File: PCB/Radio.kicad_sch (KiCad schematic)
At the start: 31 parts, among them J701 Conn_Coaxial, U701 SX1262, U702 SKY13453-385LF, Y701 NX2016SA-32MHZ-STD-CZS-5

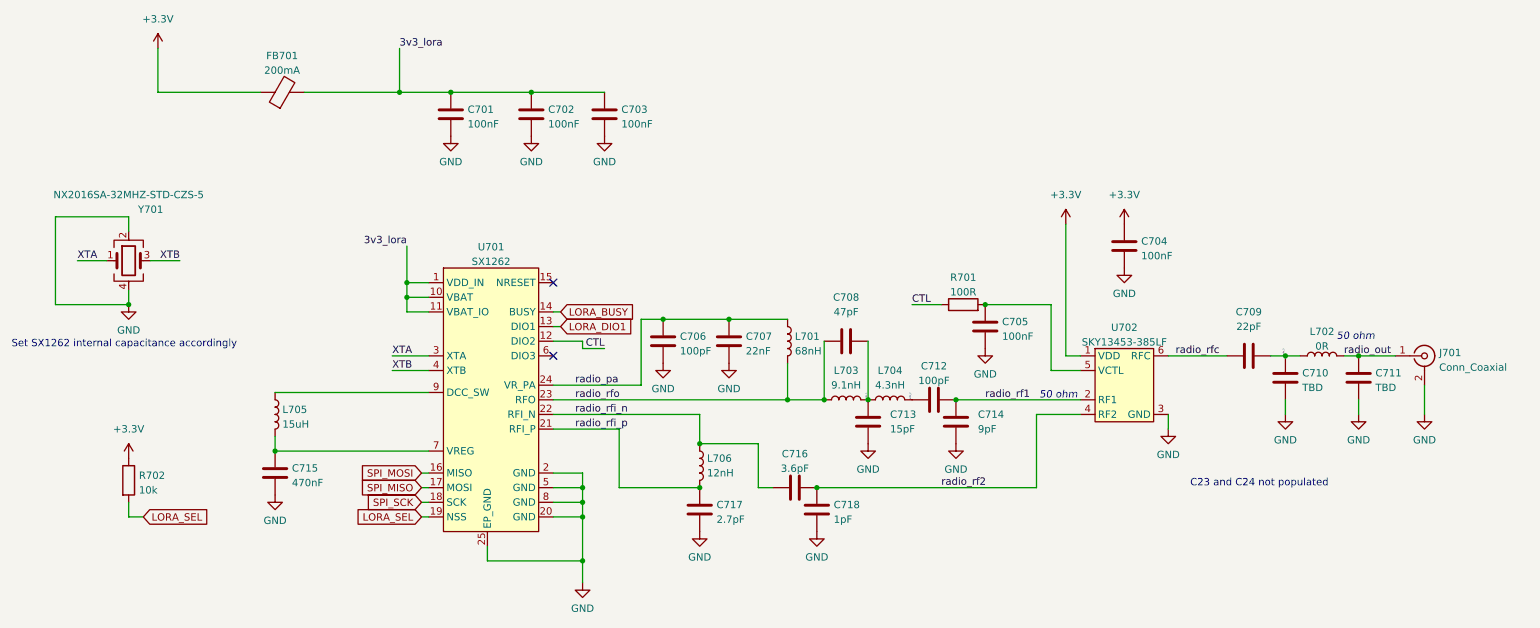
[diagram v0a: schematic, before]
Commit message: Created Bill of materials for the computer
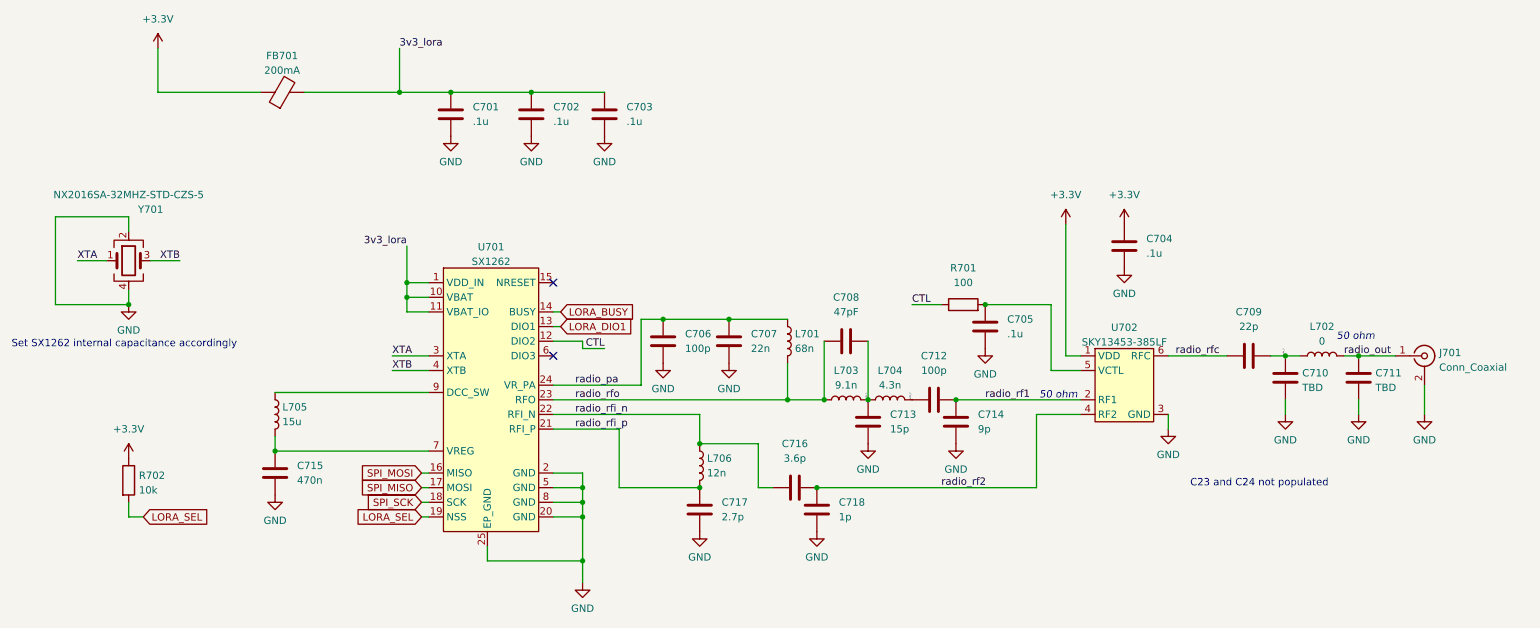
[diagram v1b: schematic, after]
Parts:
- C701, C702, C703, C704, C705: value 100nF -> .1u
- C706, C712: value 100pF -> 100p
- C707: value 22nF -> 22n
- C709: value 22pF -> 22p
- C713: value 15pF -> 15p
- C714: value 9pF -> 9p
- C715: value 470nF -> 470n
- C716: value 3.6pF -> 3.6p
- C717: value 2.7pF -> 2.7p
- C718: value 1pF -> 1p
- L701: value 68nH -> 68n
- L702: value 0R -> 0
- L703: value 9.1nH -> 9.1n
- L704: value 4.3nH -> 4.3n
- L705: value 15uH -> 15u
- L706: value 12nH -> 12n
- R701: value 100R -> 100
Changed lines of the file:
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@@
 		(fields_autoplaced yes)
 		(property "Reference" "L706"
-			(at 147.32 110.49 0)
+			(at 147.32 110.4899 0)
 			(effects
 				(font
@@
 			)
 		)
-		(property "Value" "12nH"
-			(at 147.32 113.03 0)
+		(property "Value" "12n"
+			(at 147.32 113.0299 0)
 			(effects
 				(font
@@
 		(fields_autoplaced yes)
 		(property "Reference" "C715"
-			(at 75.311 112.1953 0)
+			(at 76.2 111.7599 0)
 			(effects
 				(font
@@
 			)
 		)
-		(property "Value" "470nF"
-			(at 75.311 114.7322 0)
+		(property "Value" "470n"
+			(at 76.2 114.2999 0)
 			(effects
 				(font
@@
 		(fields_autoplaced yes)
 		(property "Reference" "C701"
-			(at 105.791 49.9653 0)
+			(at 106.68 49.5299 0)
 			(effects
 				(font
@@
 			)
 		)
-		(property "Value" "100nF"
-			(at 105.791 52.5022 0)
+		(property "Value" ".1u"
+			(at 106.68 52.0699 0)
 			(effects
 				(font
@@
 		(fields_autoplaced yes)
 		(property "Reference" "C712"
-			(at 186.69 94.4712 90)
+			(at 186.69 92.71 90)
 			(effects
 				(font
@@
 			)
 		)
-		(property "Value" "100pF"
-			(at 186.69 97.0081 90)
+		(property "Value" "100p"
+			(at 186.69 95.25 90)
 			(effects
 				(font
@@
 		(fields_autoplaced yes)
 		(property "Reference" "C707"
-			(at 154.051 89.3353 0)
+			(at 154.94 88.8999 0)
 			(effects
 				(font
@@
 			)
 		)
-		(property "Value" "22nF"
-			(at 154.051 91.8722 0)
+		(property "Value" "22n"
+			(at 154.94 91.4399 0)
 			(effects
 				(font
@@
 		(fields_autoplaced yes)
 		(property "Reference" "C705"
-			(at 198.501 86.7953 0)
+			(at 199.39 86.3599 0)
 			(effects
 				(font
@@
 			)
 		)
-		(property "Value" "100nF"
-			(at 198.501 89.3322 0)
+		(property "Value" ".1u"
+			(at 199.39 88.8999 0)
 			(effects
 				(font
@@
 		(fields_autoplaced yes)
 		(property "Reference" "L701"
-			(at 162.56 89.3353 0)
+			(at 162.56 88.8999 0)
 			(effects
 				(font
@@
 			)
 		)
-		(property "Value" "68nH"
-			(at 162.56 91.8722 0)
+		(property "Value" "68n"
+			(at 162.56 91.4399 0)
 			(effects
 				(font
@@
 		(fields_autoplaced yes)
 		(property "Reference" "C714"
-			(at 194.31 102.87 0)
+			(at 194.31 102.8699 0)
 			(effects
 				(font
@@
 			)
 		)
-		(property "Value" "9pF"
-			(at 194.31 105.41 0)
+		(property "Value" "9p"
+			(at 194.31 105.4099 0)
 			(effects
 				(font
@@
 		(fields_autoplaced yes)
 		(property "Reference" "C703"
-			(at 132.461 49.9653 0)
+			(at 133.35 49.5299 0)
 			(effects
 				(font
@@
 			)
 		)
-		(property "Value" "100nF"
-			(at 132.461 52.5022 0)
+		(property "Value" ".1u"
+			(at 133.35 52.0699 0)
 			(effects
 				(font
@@
 		(fields_autoplaced yes)
 		(property "Reference" "L702"
-			(at 254 88.5022 90)
+			(at 254 87.63 90)
 			(effects
 				(font
@@
 			)
 		)
-		(property "Value" "0R"
-			(at 254 91.0391 90)
+		(property "Value" "0"
+			(at 254 90.17 90)
 			(effects
 				(font
@@
 		(fields_autoplaced yes)
 		(property "Reference" "C706"
-			(at 142.621 89.3353 0)
+			(at 143.51 88.8999 0)
 			(effects
 				(font
@@
 			)
 		)
-		(property "Value" "100pF"
-			(at 142.621 91.8722 0)
+		(property "Value" "100p"
+			(at 143.51 91.4399 0)
 			(effects
 				(font
@@
 			)
 		)
-		(property "Value" "9.1nH"
+		(property "Value" "9.1n"
 			(at 171.45 97.79 90)
 			(effects
@@
 		(fields_autoplaced yes)
 		(property "Reference" "C716"
-			(at 162.56 109.7112 90)
+			(at 162.56 107.95 90)
 			(effects
 				(font
@@
 			)
 		)
-		(property "Value" "3.6pF"
-			(at 162.56 112.2481 90)
+		(property "Value" "3.6p"
+			(at 162.56 110.49 90)
 			(effects
 				(font
@@
 			)
 		)
-		(property "Value" "22pF"
+		(property "Value" "22p"
 			(at 241.3 87.63 90)
 			(effects
@@
 		(fields_autoplaced yes)
 		(property "Reference" "C717"
-			(at 148.971 118.5453 0)
+			(at 149.86 118.1099 0)
 			(effects
 				(font
@@
 			)
 		)
-		(property "Value" "2.7pF"
-			(at 148.971 121.0822 0)
+		(property "Value" "2.7p"
+			(at 149.86 120.6499 0)
 			(effects
 				(font
@@
 		(fields_autoplaced yes)
 		(property "Reference" "R701"
-			(at 191.77 79.1042 90)
+			(at 191.77 77.47 90)
 			(effects
 				(font
@@
 			)
 		)
-		(property "Value" "100R"
-			(at 191.77 81.6411 90)
+		(property "Value" "100"
+			(at 191.77 80.01 90)
 			(effects
 				(font
@@
 		(fields_autoplaced yes)
 		(property "Reference" "C704"
-			(at 222.631 72.8253 0)
+			(at 223.52 72.3899 0)
 			(effects
 				(font
@@
 			)
 		)
-		(property "Value" "100nF"
-			(at 222.631 75.3622 0)
+		(property "Value" ".1u"
+			(at 223.52 74.9299 0)
 			(effects
 				(font
@@
 		(fields_autoplaced yes)
 		(property "Reference" "C718"
-			(at 169.291 118.5453 0)
+			(at 170.18 118.1099 0)
 			(effects
 				(font
@@
 			)
 		)
-		(property "Value" "1pF"
-			(at 169.291 121.0822 0)
+		(property "Value" "1p"
+			(at 170.18 120.6499 0)
 			(effects
 				(font
@@
 		(fields_autoplaced yes)
 		(property "Reference" "C702"
-			(at 119.761 49.9653 0)
+			(at 120.65 49.5299 0)
 			(effects
 				(font
@@
 			)
 		)
-		(property "Value" "100nF"
-			(at 119.761 52.5022 0)
+		(property "Value" ".1u"
+			(at 120.65 52.0699 0)
 			(effects
 				(font
@@
 		(fields_autoplaced yes)
 		(property "Reference" "C713"
-			(at 179.07 102.87 0)
+			(at 179.07 102.8699 0)
 			(effects
 				(font
@@
 			)
 		)
-		(property "Value" "15pF"
-			(at 179.07 105.41 0)
+		(property "Value" "15p"
+			(at 179.07 105.4099 0)
 			(effects
 				(font
@@
 			)
 		)
-		(property "Value" "4.3nH"
+		(property "Value" "4.3n"
 			(at 179.07 97.79 90)
 			(effects
@@
 		(fields_autoplaced yes)
 		(property "Reference" "L705"
-			(at 73.66 102.0353 0)
+			(at 73.66 101.5999 0)
 			(effects
 				(font
@@
 			)
 		)
-		(property "Value" "15uH"
-			(at 73.66 104.5722 0)
+		(property "Value" "15u"
+			(at 73.66 104.1399 0)
 			(effects
 				(font

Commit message: Cleaned up the schematic and replace and rerouted everything, also replace radio with a module
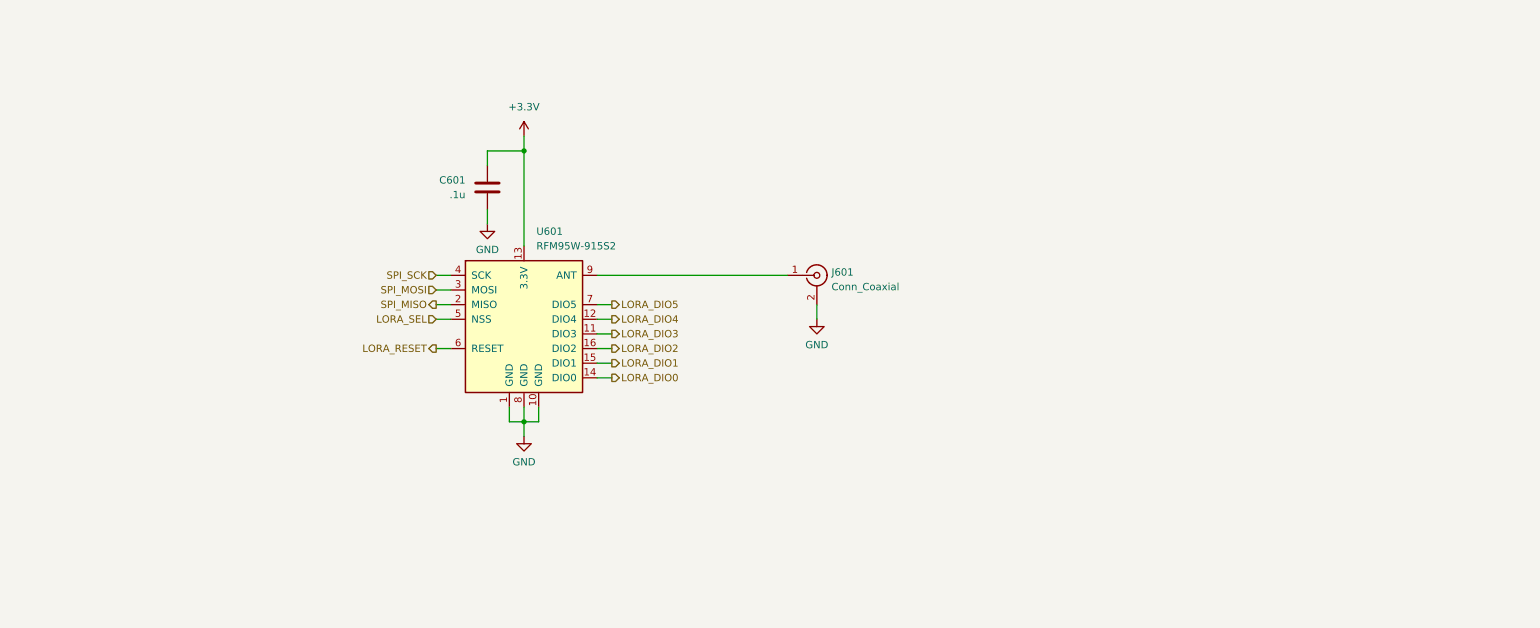
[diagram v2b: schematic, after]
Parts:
- removed C701, C702, C703, C704, C705: .1u, Capacitor_SMD:C_0603_1608Metric_Pad1.08x0.95mm_HandSolder, symbol Device:C
- removed C706, C712: 100p, Capacitor_SMD:C_0603_1608Metric_Pad1.08x0.95mm_HandSolder, symbol Device:C
- removed C707: 22n, Capacitor_SMD:C_0603_1608Metric_Pad1.08x0.95mm_HandSolder, symbol Device:C
- removed C708: 47pF, Capacitor_SMD:C_0603_1608Metric_Pad1.08x0.95mm_HandSolder, symbol Device:C
- removed C709: 22p, Capacitor_SMD:C_0603_1608Metric_Pad1.08x0.95mm_HandSolder, symbol Device:C
- removed C710, C711: TBD, Capacitor_SMD:C_0603_1608Metric_Pad1.08x0.95mm_HandSolder, symbol Device:C
- removed C713: 15p, Capacitor_SMD:C_0603_1608Metric_Pad1.08x0.95mm_HandSolder, symbol Device:C
- removed C714: 9p, Capacitor_SMD:C_0603_1608Metric_Pad1.08x0.95mm_HandSolder, symbol Device:C
- removed C715: 470n, Capacitor_SMD:C_0603_1608Metric_Pad1.08x0.95mm_HandSolder, symbol Device:C
- removed C716: 3.6p, Capacitor_SMD:C_0603_1608Metric_Pad1.08x0.95mm_HandSolder, symbol Device:C
- removed C717: 2.7p, Capacitor_SMD:C_0603_1608Metric_Pad1.08x0.95mm_HandSolder, symbol Device:C
- removed C718: 1p, Capacitor_SMD:C_0603_1608Metric_Pad1.08x0.95mm_HandSolder, symbol Device:C
- removed FB701: 200mA, Inductor_SMD:L_0603_1608Metric, symbol Device:FerriteBead
- removed L701: 68n, Inductor_SMD:L_0603_1608Metric_Pad1.05x0.95mm_HandSolder, symbol Device:L
- removed L702: 0, Inductor_SMD:L_0603_1608Metric_Pad1.05x0.95mm_HandSolder, symbol Device:L
- removed L703: 9.1n, Inductor_SMD:L_0603_1608Metric_Pad1.05x0.95mm_HandSolder, symbol Device:L
- removed L704: 4.3n, Inductor_SMD:L_0603_1608Metric_Pad1.05x0.95mm_HandSolder, symbol Device:L
- removed L705: 15u, Inductor_SMD:L_0603_1608Metric_Pad1.05x0.95mm_HandSolder, symbol Device:L
- removed L706: 12n, Inductor_SMD:L_0603_1608Metric_Pad1.05x0.95mm_HandSolder, symbol Device:L
- removed R701: 100, Resistor_SMD:R_0603_1608Metric_Pad0.98x0.95mm_HandSolder, symbol Device:R
- removed R702: 10k, Resistor_SMD:R_0603_1608Metric_Pad0.98x0.95mm_HandSolder, symbol Device:R
- removed U701: SX1262, Package_DFN_QFN:QFN-24-1EP_4x4mm_P0.5mm_EP2.7x2.7mm, symbol stanley_misc:SX1262
- removed U702: SKY13453-385LF, imported:QFN_453-385LF_SKY, symbol stanley_misc:SKY13453-385LF
- removed Y701: NX2016SA-32MHZ-STD-CZS-5, Crystal:Crystal_SMD_2016-4Pin_2.0x1.6mm, symbol Device:Crystal_GND24
- added C601: .1u, Capacitor_SMD:C_0603_1608Metric, symbol Device:C
- added U601: RFM95W-915S2, RF_Module:HOPERF_RFM9XW_SMD, symbol RF_Module:RFM95W-915S2
- renumbered J701 to J601
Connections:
- net +3.3V: now also C601.1, U601.13 (3.3V)
- net GND: now also C601.2, U601.1 (GND), U601.10 (GND), U601.8 (GND)
- net LORA_DIO1: now also U601.15 (DIO1)
- net LORA_SEL: now also U601.5 (NSS)
- net SPI_MISO: now also U601.2 (MISO)
- net SPI_MOSI: now also U601.3 (MOSI)
- net SPI_SCK: now also U601.4 (SCK)
- net radio_out: no longer names the net of J601.1 (In)
- net radio_out: now also U601.9 (ANT)
- new net LORA_DIO0: U601.14 (DIO0)
- new net LORA_DIO2: U601.16 (DIO2)
- new net LORA_DIO3: U601.11 (DIO3)
- new net LORA_DIO4: U601.12 (DIO4)
- new net LORA_DIO5: U601.7 (DIO5)
- new net LORA_RESET: U601.6 (RESET)
- no-connect marks 2 -> 0
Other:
- note removed: "50 ohm"
- note removed: "C23 and C24 not populated"
- note removed: "Set SX1262 internal capacitance accordingly"
- moved on the sheet: J601

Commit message: Updated BOM and fixed all ERC and DRC errors
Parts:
- C601: footprint Capacitor_SMD:C_0603_1608Metric -> Capacitor_SMD:C_0603_1608Metric_Pad1.08x0.95mm_HandSolder
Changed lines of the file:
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@@
 			)
 		)
-		(property "Footprint" "Capacitor_SMD:C_0603_1608Metric"
+		(property "Footprint" "Capacitor_SMD:C_0603_1608Metric_Pad1.08x0.95mm_HandSolder"
 			(at 110.1852 67.31 0)
 			(effects

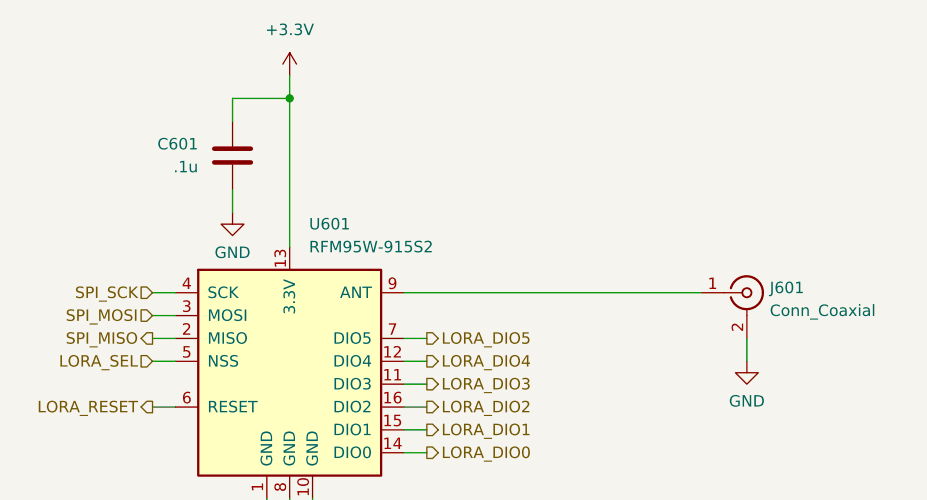
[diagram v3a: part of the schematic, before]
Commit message: Switch from high side switch to low side switch for pyro channels
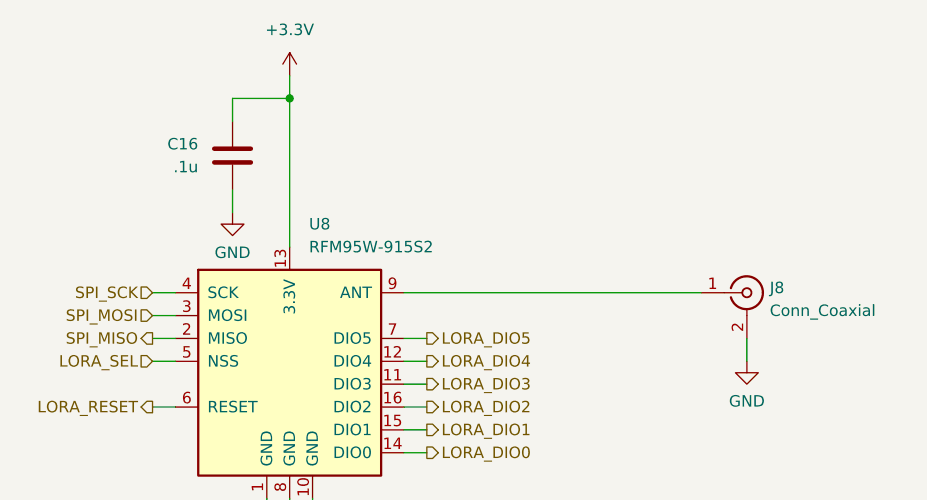
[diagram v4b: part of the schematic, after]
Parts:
- renumbered C601 to C16, J601 to J8, U601 to U8
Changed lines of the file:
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@@
 		(dnp no)
 		(fields_autoplaced yes)
-		(property "Reference" "#PWR0601"
+		(property "Reference" "#PWR056"
 			(at 115.57 58.42 0)
 			(effects
@@
 			(project "Flight Computer"
 				(path "/4254ccd1-49f4-4fe6-9bf7-ccb200d73af4/b5b3f2b6-4604-4088-8488-54d61b2ee536"
-					(reference "#PWR0601")
+					(reference "#PWR056")
 					(unit 1)
 				)
@@
 		(dnp no)
 		(fields_autoplaced yes)
-		(property "Reference" "#PWR0602"
+		(property "Reference" "#PWR057"
 			(at 109.22 76.2 0)
 			(effects
@@
 			(project "Flight Computer"
 				(path "/4254ccd1-49f4-4fe6-9bf7-ccb200d73af4/b5b3f2b6-4604-4088-8488-54d61b2ee536"
-					(reference "#PWR0602")
+					(reference "#PWR057")
 					(unit 1)
 				)
@@
 		(on_board yes)
 		(dnp no)
-		(property "Reference" "C601"
+		(property "Reference" "C16"
 			(at 105.41 62.2299 0)
 			(effects
@@
 			(project ""
 				(path "/4254ccd1-49f4-4fe6-9bf7-ccb200d73af4/b5b3f2b6-4604-4088-8488-54d61b2ee536"
-					(reference "C601")
+					(reference "C16")
 					(unit 1)
 				)
@@
 		(dnp no)
 		(fields_autoplaced yes)
-		(property "Reference" "J601"
+		(property "Reference" "J8"
 			(at 168.91 78.1985 0)
 			(effects
@@
 			(project "Flight Computer"
 				(path "/4254ccd1-49f4-4fe6-9bf7-ccb200d73af4/b5b3f2b6-4604-4088-8488-54d61b2ee536"
-					(reference "J601")
+					(reference "J8")
 					(unit 1)
 				)
@@
 		(dnp no)
 		(fields_autoplaced yes)
-		(property "Reference" "U601"
+		(property "Reference" "U8"
 			(at 117.7133 71.12 0)
 			(effects
@@
 			(project ""
 				(path "/4254ccd1-49f4-4fe6-9bf7-ccb200d73af4/b5b3f2b6-4604-4088-8488-54d61b2ee536"
-					(reference "U601")
+					(reference "U8")
 					(unit 1)
 				)
@@
 		(dnp no)
 		(fields_autoplaced yes)
-		(property "Reference" "#PWR0604"
+		(property "Reference" "#PWR059"
 			(at 115.57 113.03 0)
 			(effects
@@
 			(project "Flight Computer"
 				(path "/4254ccd1-49f4-4fe6-9bf7-ccb200d73af4/b5b3f2b6-4604-4088-8488-54d61b2ee536"
-					(reference "#PWR0604")
+					(reference "#PWR059")
 					(unit 1)
 				)
@@
 		(dnp no)
 		(fields_autoplaced yes)
-		(property "Reference" "#PWR0603"
+		(property "Reference" "#PWR058"
 			(at 166.37 92.71 0)
 			(effects
@@
 			(project "Flight Computer"
 				(path "/4254ccd1-49f4-4fe6-9bf7-ccb200d73af4/b5b3f2b6-4604-4088-8488-54d61b2ee536"
-					(reference "#PWR0603")
-					(unit 1)
-				)
+					(reference "#PWR058")
+					(unit 1)
+				)
